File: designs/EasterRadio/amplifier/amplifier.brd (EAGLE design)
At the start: 38 x 35 mm, 15 parts, among them J1 S2B-NSHSS-TB, J2 S2B-NSHSS-TB

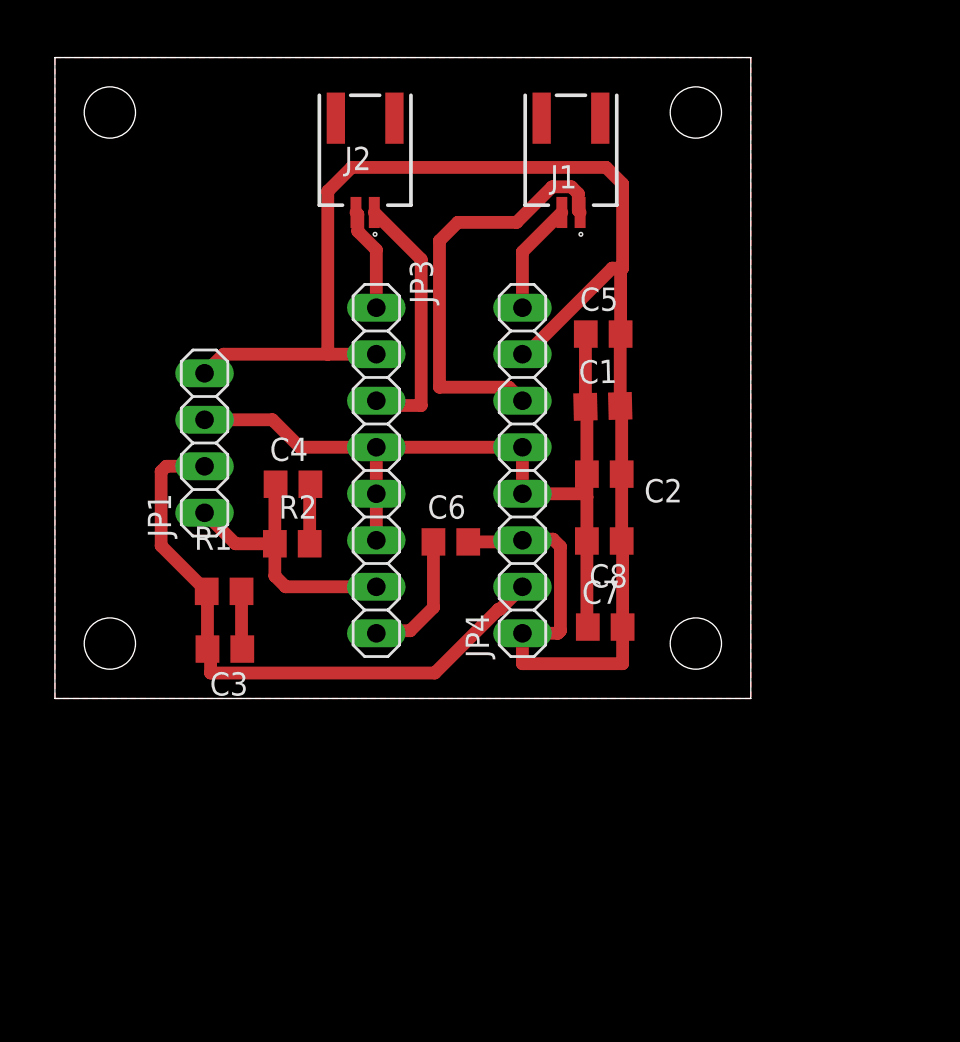
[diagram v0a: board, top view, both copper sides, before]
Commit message: added amplifier with stereo jack
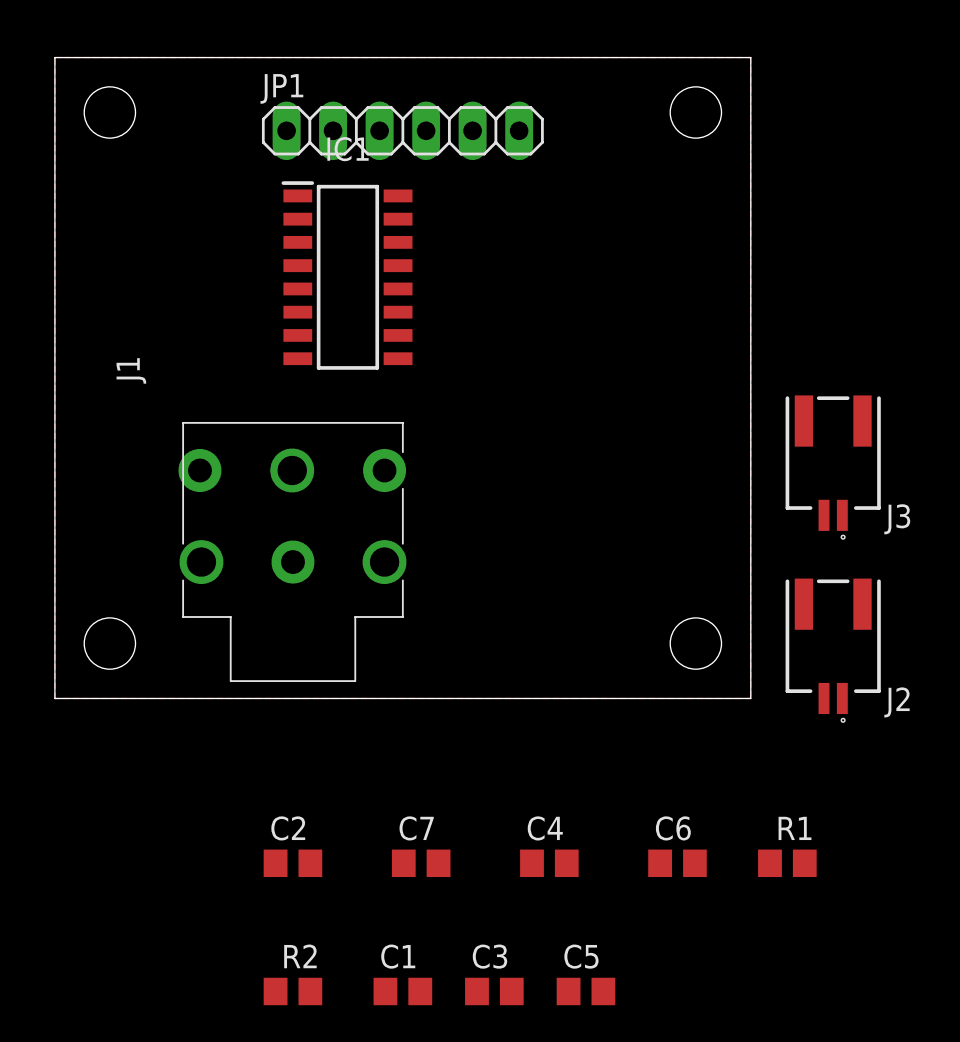
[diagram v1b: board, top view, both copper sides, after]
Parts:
- removed C8: 470uF, CommonParts:C0805
- removed JP3, JP4: (no value), pinhead:1X08
- added IC1: PAM8403DR, MouserUseful:SOIC127P605X175-16N
- added J3: S2B-NSHSS-TB, CommonParts:SM02B-NSHSS-TB
- C2: value 1uF -> 0.47uF
- C3: value 0.47uF -> 1uF
- C4: value 0.47uF -> 470uF
- C7: value 470uF -> 0.47uF
- J1: value S2B-NSHSS-TB -> STX-3120-3BM; device CommonParts:SM02B-NSHSS-TB -> MouserUseful:STX31203BM
- JP1: device pinhead:1X04 -> pinhead:1X06
- moved J2 36.8 mm to (42.0, 0.00)
- moved C5 35.9 mm to (29.0, -16.0)
- moved R1 34.2 mm to (40.0, -9.00)
- moved C1 33.8 mm to (19.0, -16.0), turned to 0 degrees
- moved C2 27.2 mm to (13.0, -9.00), turned to 0 degrees
- moved C4 25.0 mm to (27.0, -9.00)
- moved R2 24.5 mm to (13.0, -16.0)
- moved C3 23.8 mm to (24.0, -16.0), turned to 0 degrees
- moved J1 23.6 mm to (13.0, 8.00), turned to 90 degrees
- moved C6 21.5 mm to (34.0, -9.00)
- moved JP1 20.2 mm to (19.0, 31.0), turned to 0 degrees
- moved C7 16.4 mm to (20.0, -9.00)
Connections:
- removed net +OUT_L: J2.2, JP3.1
- removed net +OUT_R: J1.2, JP4.8
- removed net -OUT_L: J2.1, JP3.3
- removed net -OUT_R: J1.1, JP4.6
- removed net N$1: C3.1, R1.2
- removed net N$4: C4.2, R2.2
- removed net VREF: C6.1, JP3.8
- new net !MUTE: IC1.5
- new net !SHDN: IC1.12
- new net IC2_INL: IC1.7, R1.1
- new net IC2_INR: IC1.10, R2.1
- new net IC2_VREF: C6.1, IC1.8
- new net N$11: C2.2, R1.2
- new net N$12: C7.1, R2.2
- new net N$15: JP1.5
- new net N$16: JP1.4
- new net N$17: JP1.3
- new net N$18: JP1.2
- new net OUT_L+: IC1.1, J3.2
- new net OUT_L-: IC1.3, J3.1
- new net OUT_R+: IC1.16, J2.2
- new net OUT_R-: IC1.14, J2.1
- net 3.3V: now also C3.1, C4.1, IC1.13, IC1.4, IC1.6, JP1.6; no longer C2.2, C7.1, C8.2, JP1.3, JP3.4, JP3.5, JP3.6, JP4.4, JP4.5
- net AGND: now also C3.2, C4.2, IC1.11, IC1.15, IC1.2, IC1.9, J1.1, JP1.1; no longer C2.1, C7.2, C8.1, JP1.4, JP3.2, JP4.1, JP4.3, JP4.7
- net INL: now also C2.1, J1.2; no longer C4.1, JP1.1, JP3.7, R2.1
- net INR: now also C7.2, J1.5; no longer C3.2, JP1.2, JP4.2, R1.1
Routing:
- net AGND: track 88.9 -> 0.00 mm
- net 3.3V: track 45.5 -> 0.00 mm
- net INR: track 33.8 -> 0.00 mm
- net -OUT_R: track 22.9 -> 0.00 mm
- net INL: track 15.4 -> 0.00 mm
- net -OUT_L: track 14.2 -> 0.00 mm
- net VREF: track 7.28 -> 0.00 mm
- net +OUT_R: track 6.09 -> 0.00 mm
- net +OUT_L: track 5.66 -> 0.00 mm
- net N$4: track 3.27 -> 0.00 mm
- net N$1: track 3.22 -> 0.00 mm

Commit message: added amplifier brd
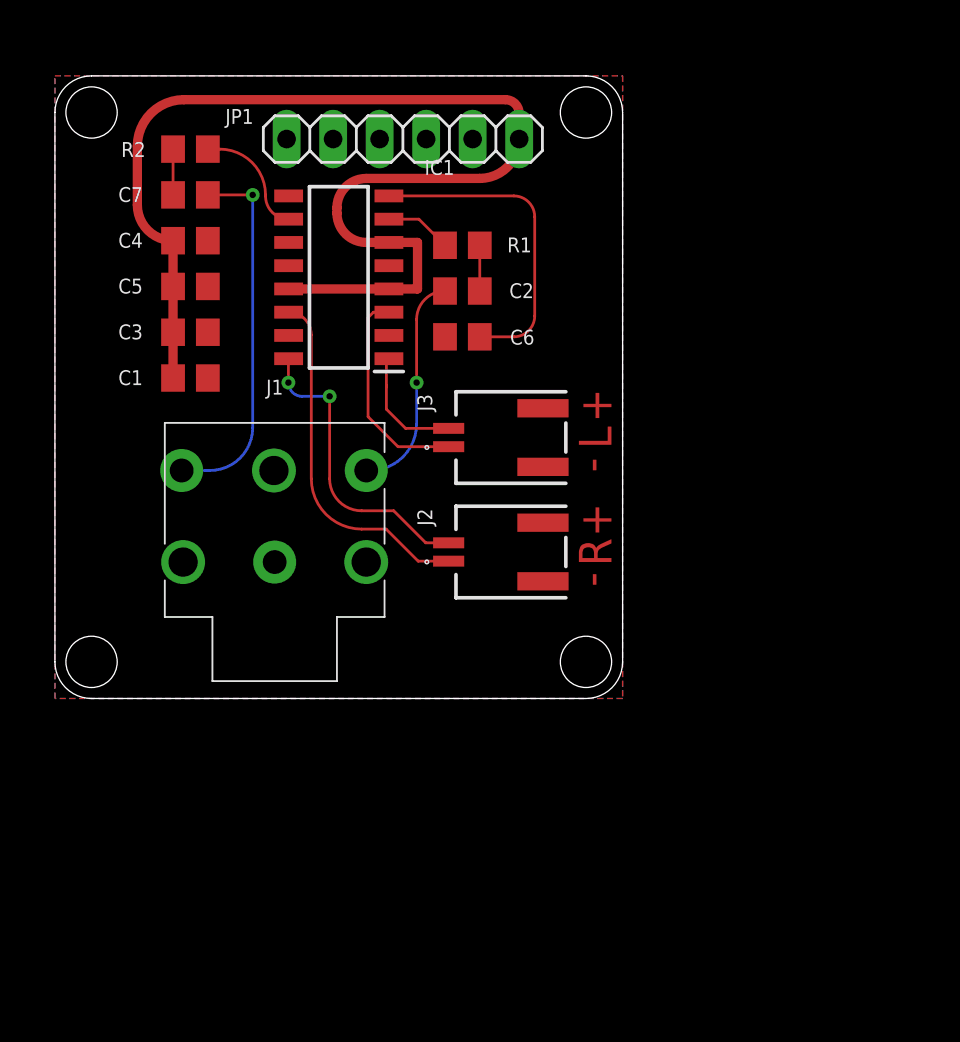
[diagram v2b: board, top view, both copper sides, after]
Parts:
- moved R2 46.3 mm to (7.40, 30.0), turned to 180 degrees
- moved C5 44.1 mm to (7.40, 22.5)
- moved C3 39.6 mm to (7.40, 20.0)
- moved C4 39.2 mm to (7.40, 25.0)
- moved C7 38.6 mm to (7.40, 27.5)
- moved R1 38.1 mm to (22.2, 24.8)
- moved C1 35.5 mm to (7.40, 17.5)
- moved C2 32.6 mm to (22.2, 22.2)
- moved C6 31.1 mm to (22.2, 19.8), turned to 180 degrees
- moved J2 22.2 mm to (21.5, 8.50), turned to 270 degrees
- moved J3 21.0 mm to (21.5, 14.8), turned to 270 degrees
- moved J1 1.00 mm to (12.0, 8.00)
- moved IC1 0.50 mm to (15.5, 23.0), turned to 180 degrees
- moved JP1 0.45 mm to (19.0, 30.6)
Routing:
- net 3.3V: track 0.00 -> 63.6 mm
- net INR: track 0.00 -> 20.0 mm, vias 0 -> 1
- net OUT_R-: track 0.00 -> 19.0 mm
- net IC2_VREF: track 0.00 -> 17.3 mm
- net OUT_R+: track 0.00 -> 16.3 mm, vias 0 -> 2
- net OUT_L-: track 0.00 -> 11.8 mm
- net INL: track 0.00 -> 11.7 mm, vias 0 -> 1
- net OUT_L+: track 0.00 -> 6.65 mm
- net IC2_INR: track 0.00 -> 6.03 mm
- net IC2_INL: track 0.00 -> 3.65 mm
- net N$12: track 0.00 -> 2.50 mm
- net N$11: track 0.00 -> 2.50 mm
- added copper zone on layer 16, net AGND
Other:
- board size 38 x 35 mm -> 31 x 34 mm
- board text added: "+"
- board text added: "-"
- board text added: "L"
- board text added: "R"

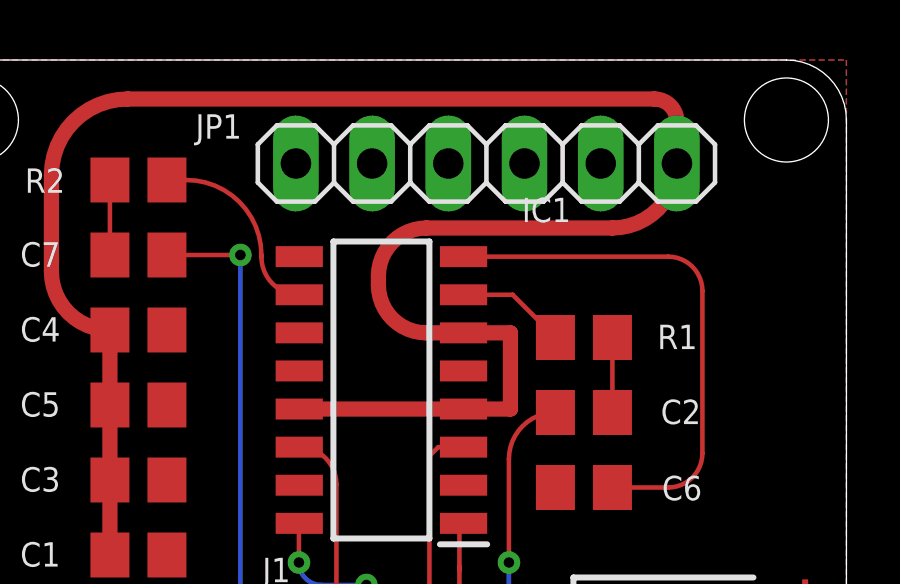
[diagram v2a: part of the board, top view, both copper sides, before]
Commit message: added amplifier brd
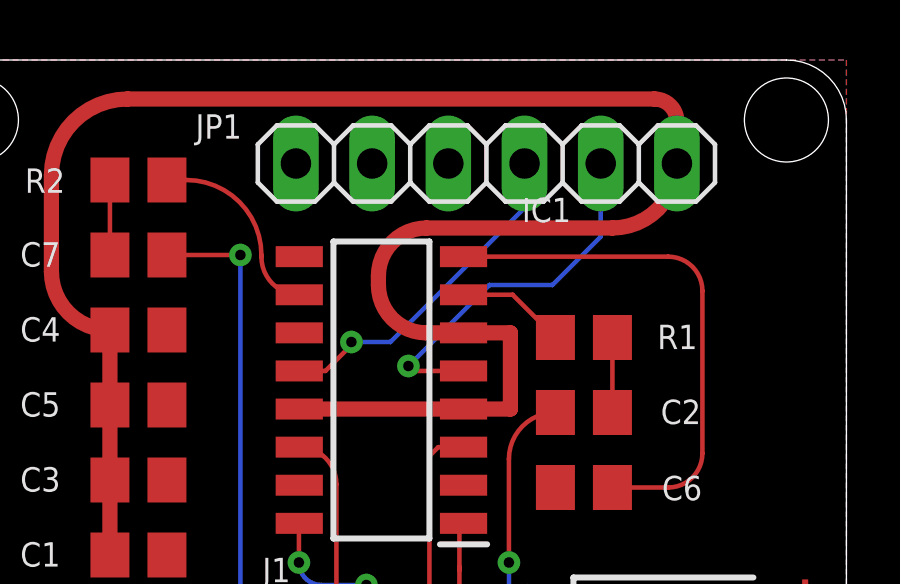
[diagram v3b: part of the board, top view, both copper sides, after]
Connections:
- removed net N$15: JP1.5
- removed net N$16: JP1.4
- net !MUTE: now also JP1.5
- net !SHDN: now also JP1.4
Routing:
- net !MUTE: track 0.00 -> 12.5 mm, vias 0 -> 1
- net !SHDN: track 0.00 -> 11.3 mm, vias 0 -> 1
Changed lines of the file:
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@@
 <setting verticaltext="up"/>
 </settings>
-<grid distance="1" unitdist="mm" unit="mm" style="lines" multiple="1" display="yes" altdistance="5" altunitdist="mil" altunit="mil"/>
+<grid distance="0.1" unitdist="mm" unit="mm" style="lines" multiple="1" display="yes" altdistance="5" altunitdist="mil" altunit="mil"/>
 <layers>
 <layer number="1" name="Top" color="4" fill="1" visible="yes" active="yes"/>
@@
 <signal name="!MUTE">
 <contactref element="IC1" pad="5"/>
+<contactref element="JP1" pad="5"/>
+<wire x1="18.238" y1="23.635" x2="16.565" y2="23.635" width="0.1524" layer="1"/>
+<wire x1="16.565" y1="23.635" x2="16.4" y2="23.8" width="0.1524" layer="1"/>
+<via x="16.4" y="23.8" extent="1-16" drill="0.35"/>
+<wire x1="16.4" y1="23.8" x2="19.1" y2="26.5" width="0.1524" layer="16"/>
+<wire x1="19.1" y1="26.5" x2="21.2" y2="26.5" width="0.1524" layer="16"/>
+<wire x1="21.2" y1="26.5" x2="22.81" y2="28.11" width="0.1524" layer="16"/>
+<wire x1="22.81" y1="28.11" x2="22.81" y2="30.55" width="0.1524" layer="16"/>
 </signal>
 <signal name="IC2_INL">
@@
 <signal name="!SHDN">
 <contactref element="IC1" pad="12"/>
+<contactref element="JP1" pad="4"/>
+<wire x1="12.762" y1="23.635" x2="13.635" y2="23.635" width="0.1524" layer="1"/>
+<wire x1="14.5" y1="24.5" x2="14.5" y2="24.6" width="0.1524" layer="1"/>
+<via x="14.5" y="24.6" extent="1-16" drill="0.35"/>
+<wire x1="14.5" y1="24.6" x2="15.8" y2="24.6" width="0.1524" layer="16"/>
+<wire x1="20.27" y1="29.07" x2="15.8" y2="24.6" width="0.1524" layer="16"/>
+<wire x1="20.27" y1="29.07" x2="20.27" y2="30.55" width="0.1524" layer="16"/>
+<wire x1="13.635" y1="23.635" x2="14.5" y2="24.5" width="0.1524" layer="1"/>
 </signal>
 <signal name="IC2_INR">
@@
 <wire x1="6.45" y1="30" x2="6.45" y2="27.5" width="0.1524" layer="1"/>
 </signal>
-<signal name="N$15">
-<contactref element="JP1" pad="5"/>
-</signal>
-<signal name="N$16">
-<contactref element="JP1" pad="4"/>
-</signal>
 <signal name="N$17">
